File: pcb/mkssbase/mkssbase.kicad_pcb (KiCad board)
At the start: 2 copper layers, 46 x 92.7 mm, 63 parts, among them IC1 74LV11, IC2 74HCT08, IC3 MAX485E, IC4 AMS1117-3.3, J1 DOOR1, J10 TO_J7, J11 24V PWR, J12 LED LIGHTING, J13 AIR VALVE, J14 AIMING LASER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

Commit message: Fix wrong supply voltage to IC1.
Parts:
- moved C3 12.3 mm to (230.5, 108.6), turned to 180 degrees
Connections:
- C4 pad 1: +5V -> +3V3
- IC1 pad 14: +5V -> +3V3
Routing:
- net GND: track 155.3 -> 345.2 mm, vias 3 -> 7
- net +3V3: track 0.00 -> 109.0 mm, vias 0 -> 7
- net Net-(C11-Pad1): track 19.1 -> 75.2 mm, vias 0 -> 1
- net Net-(J10-Pad4): track 0.00 -> 46.6 mm
- net Net-(C10-Pad1): track 0.00 -> 44.7 mm
- net +5V: track 47.3 -> 85.3 mm, vias 0 -> 1
- net Net-(D1-Pad2): track 9.06 -> 43.6 mm
- net Net-(J10-Pad6): track 0.00 -> 17.5 mm
- net P2.12: track 11.0 -> 26.9 mm, vias 1 -> 2
- net Net-(J15-Pad2): track 0.00 -> 11.2 mm
- net Net-(IC1-Pad13): track 0.00 -> 7.84 mm
- net Net-(Q1-Pad1): track 0.00 -> 2.22 mm

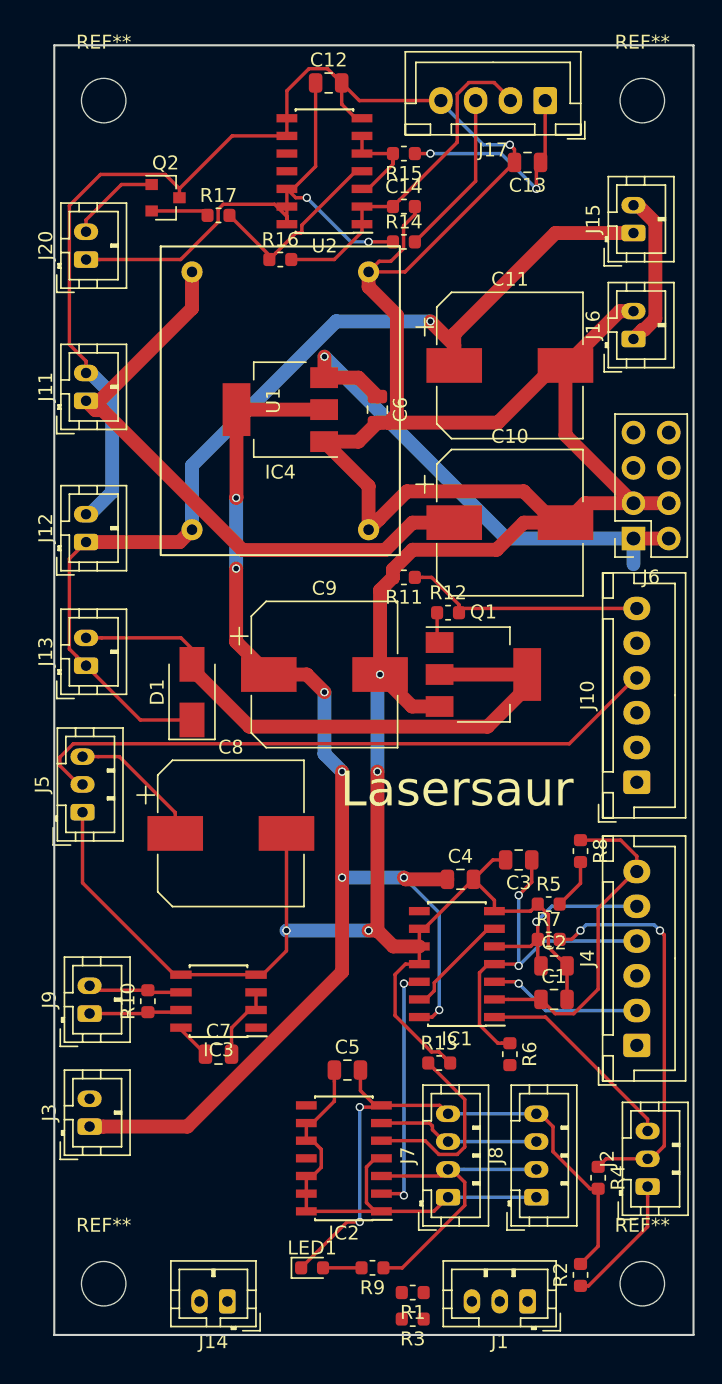
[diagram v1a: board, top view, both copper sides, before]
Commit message: Add inverted laser control signal.
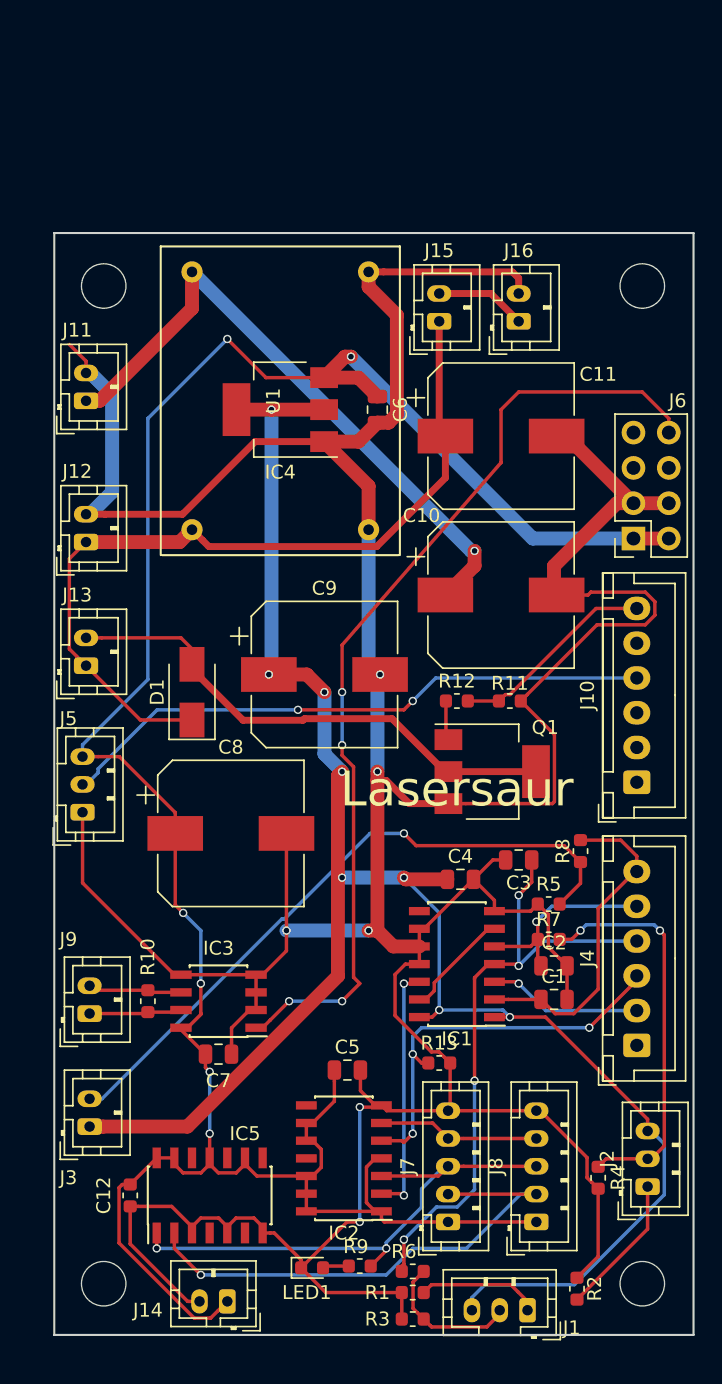
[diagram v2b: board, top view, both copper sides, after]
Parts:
- removed C13: 1u, Capacitor_SMD:C_0805_2012Metric
- removed C14: 10n, Capacitor_SMD:C_0603_1608Metric
- removed J17: Switch, Connector_JST:JST_XH_B04B-XH-A_1x04_P2.50mm_Vertical
- removed J20: SSR, Connector_JST:JST_PH_B2B-PH-K_1x02_P2.00mm_Vertical
- removed Q2: MMBT3904, Package_TO_SOT_SMD:SOT-23
- removed R14: R, Resistor_SMD:R_0603_1608Metric
- removed R15, R16: 100k, Resistor_SMD:R_0603_1608Metric
- removed R17: 10k, Resistor_SMD:R_0603_1608Metric
- removed U2: 4011, Package_SO:SOIC-14_3.9x8.7mm_P1.27mm
- added IC5: 74HCT04, Package_SO:SOIC-14_3.9x8.7mm_P1.27mm, F.Cu at (208.3, 132.7)
- C12: value 1u -> 100n; footprint Capacitor_SMD:C_0805_2012Metric -> Capacitor_SMD:C_0603_1608Metric
- J7, J8: footprint Connector_JST:JST_PH_B4B-PH-K_1x04_P2.00mm_Vertical -> Connector_JST:JST_PH_B5B-PH-K_1x05_P2.00mm_Vertical
- moved C12 81.3 mm to (202.6, 132.7), turned to 270 degrees
- moved R6 17.1 mm to (222.9, 138.2), turned to 0 degrees
- moved J15 15.3 mm to (224.8, 69.8)
- moved REF** 13.3 mm to (200.7, 67.3)
- moved REF** 13.3 mm to (239.4, 67.3)
- moved R11 11.7 mm to (229.9, 97.2), turned to 0 degrees
- moved J16 8.35 mm to (230.5, 69.8)
- moved Q1 7.01 mm to (228.6, 102.2)
- moved R12 6.38 mm to (226.1, 97.2)
- moved C10 5.25 mm to (229.2, 89.5)
- moved C11 5.12 mm to (229.2, 78.1)
- moved J7 1.78 mm to (225.4, 134.6)
- moved J8 1.78 mm to (231.8, 134.6)
- moved R2 1.02 mm to (234.7, 139.4)
- moved R9 0.92 mm to (219.1, 137.8)
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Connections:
- C12 pad 1: +12V -> +5V
- J7 pad 2: Net-(IC2-Pad3) -> Net-(IC5-Pad2)
- J7 pad 3: Net-(IC2-Pad6) -> Net-(IC2-Pad3)
- J7 pad 4: GND -> Net-(IC2-Pad6)
- J8 pad 2: Net-(IC2-Pad3) -> Net-(IC5-Pad2)
- J8 pad 3: Net-(IC2-Pad6) -> Net-(IC2-Pad3)
- J8 pad 4: GND -> Net-(IC2-Pad6)
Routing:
- net +5V: track 85.3 -> 180.0 mm, vias 1 -> 6
- net RX: track 0.00 -> 69.3 mm, vias 0 -> 4
- net Net-(J3-Pad2): track 3.64 -> 47.7 mm, vias 0 -> 1
- net +12V: track 38.0 -> 0.00 mm, vias 2 -> 0
- net Net-(IC5-Pad2): track 0.00 -> 36.7 mm, vias 0 -> 1
- net +3V3: track 109.0 -> 135.8 mm, vias 7 -> 8
- net Net-(C14-Pad1): track 24.7 -> 0.00 mm
- net P2.12: track 26.9 -> 44.7 mm, vias 2 -> 4
- net Net-(C13-Pad1): track 16.4 -> 0.00 mm, vias 2 -> 0
- net Net-(IC2-Pad3): track 22.3 -> 38.7 mm, vias 0 -> 2
- net Net-(C11-Pad1): track 75.2 -> 59.3 mm, vias 1 -> 0
- net P1.23: track 13.7 -> 29.0 mm, vias 0 -> 3
- net GND: track 345.2 -> 330.3 mm, vias 7 -> 6
- net Net-(R16-Pad1): track 13.9 -> 0.00 mm
- net Net-(J17-Pad3): track 12.0 -> 0.00 mm
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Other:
- board size 46 x 92.7 mm -> 46 x 79.2 mm
- net class Power2 added: clearance 0.2, trace_width 0.5, via_dia 0.6, via_drill 0.4

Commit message: Fix overlapping silk screen.
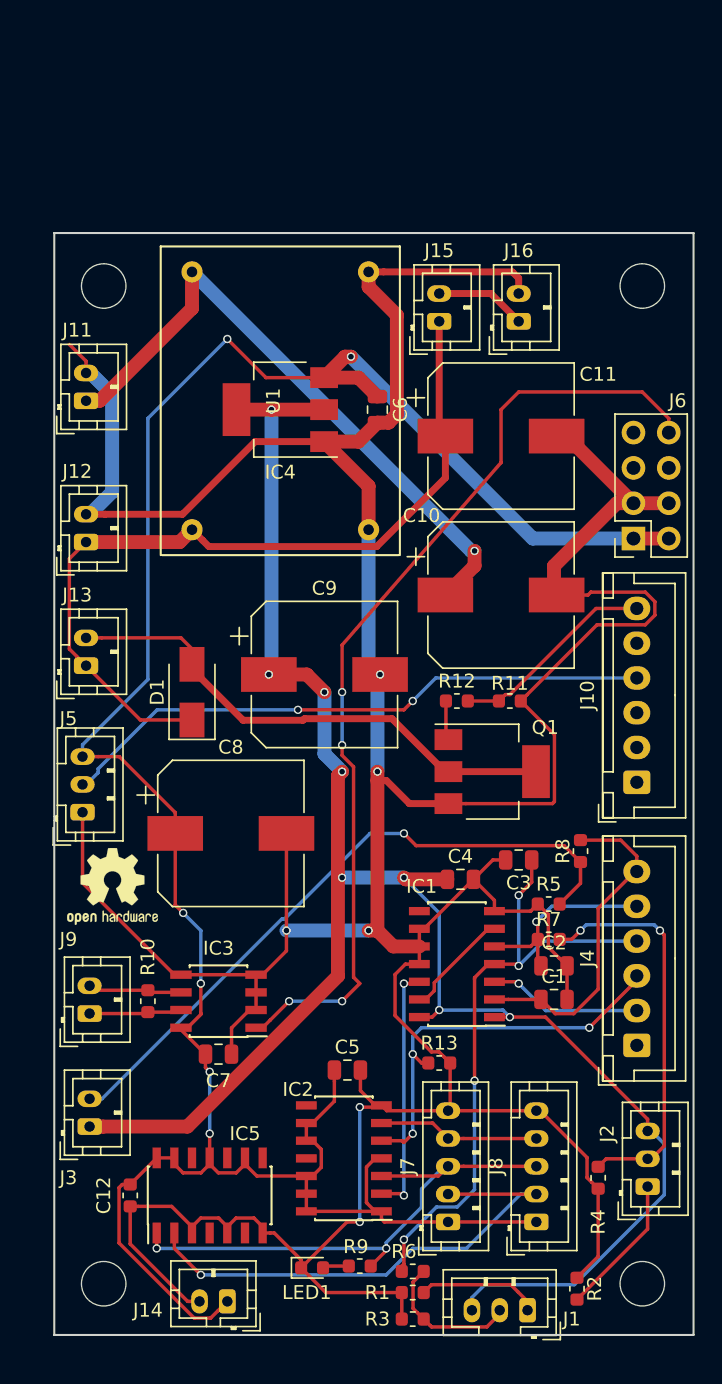
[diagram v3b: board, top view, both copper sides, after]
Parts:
- added REF**: OSHW-Logo2_7.3x6mm_SilkScreen, Symbol:OSHW-Logo2_7.3x6mm_SilkScreen, F.Cu at (201.3, 110.5)
